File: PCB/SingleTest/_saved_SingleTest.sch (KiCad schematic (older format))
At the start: 5 parts

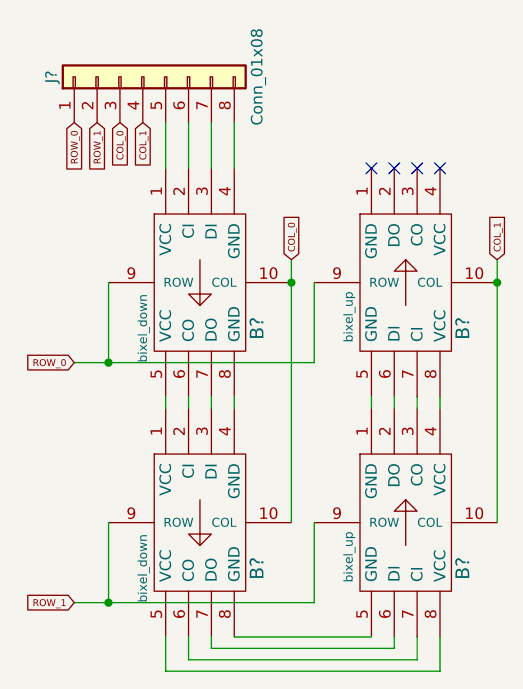
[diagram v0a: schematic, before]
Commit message: Adding single test
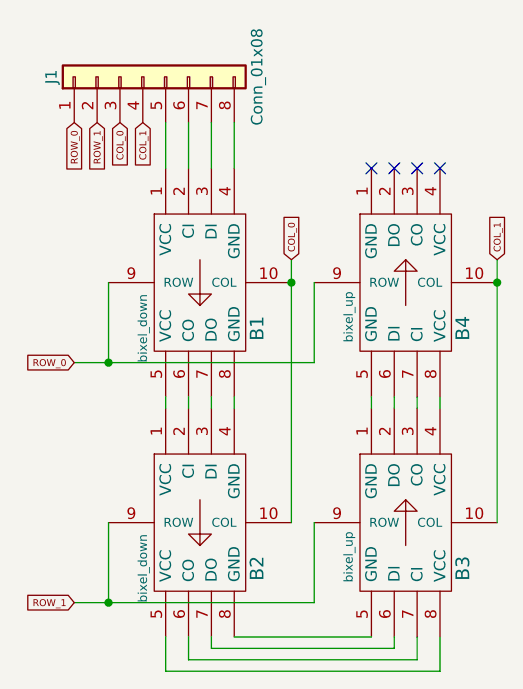
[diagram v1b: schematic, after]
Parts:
- B1, B2, B3, B4: renamed from B?; footprint (none) -> custom:bixel
- J1: renamed from J?; footprint (none) -> Socket_Strips:Socket_Strip_Straight_1x08_Pitch2.54mm
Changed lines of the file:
@@
 $EndDescr
 $Comp
-L bixel_down B?
+L bixel_down B1
 U 1 1 5B36BF26
 P 2600 3400
-F 0 "B?" V 2850 3200 60  0000 C CNN
+F 0 "B1" V 2850 3200 60  0000 C CNN
 F 1 "bixel_down" V 2350 3200 39  0000 C CNN
-F 2 "" H 2600 3400 60  0001 C CNN
+F 2 "custom:bixel" H 2600 3400 60  0001 C CNN
 F 3 "" H 2600 3400 60  0001 C CNN
 	1    2600 3400
@@
 $EndComp
 $Comp
-L bixel_up B?
+L bixel_up B4
 U 1 1 5B36BF6D
 P 3500 3400
-F 0 "B?" V 3750 3200 60  0000 C CNN
+F 0 "B4" V 3750 3200 60  0000 C CNN
 F 1 "bixel_up" V 3250 3250 39  0000 C CNN
-F 2 "" H 3500 3400 60  0001 C CNN
+F 2 "custom:bixel" H 3500 3400 60  0001 C CNN
 F 3 "" H 3500 3400 60  0001 C CNN
 	1    3500 3400
@@
 $EndComp
 $Comp
-L bixel_down B?
+L bixel_down B2
 U 1 1 5B36BFAC
 P 2600 4450
-F 0 "B?" V 2850 4250 60  0000 C CNN
+F 0 "B2" V 2850 4250 60  0000 C CNN
 F 1 "bixel_down" V 2350 4250 39  0000 C CNN
-F 2 "" H 2600 4450 60  0001 C CNN
+F 2 "custom:bixel" H 2600 4450 60  0001 C CNN
 F 3 "" H 2600 4450 60  0001 C CNN
 	1    2600 4450
@@
 $EndComp
 $Comp
-L bixel_up B?
+L bixel_up B3
 U 1 1 5B36BFD9
 P 3500 4450
-F 0 "B?" V 3750 4250 60  0000 C CNN
+F 0 "B3" V 3750 4250 60  0000 C CNN
 F 1 "bixel_up" V 3250 4300 39  0000 C CNN
-F 2 "" H 3500 4450 60  0001 C CNN
+F 2 "custom:bixel" H 3500 4450 60  0001 C CNN
 F 3 "" H 3500 4450 60  0001 C CNN
 	1    3500 4450
@@
 NoConn ~ 3650 2900
 $Comp
-L Conn_01x08 J?
+L Conn_01x08 J1
 U 1 1 5B36C3AB
 P 2350 2500
-F 0 "J?" H 2350 2900 50  0000 C CNN
+F 0 "J1" H 2350 2900 50  0000 C CNN
 F 1 "Conn_01x08" H 2350 2000 50  0000 C CNN
-F 2 "" H 2350 2500 50  0001 C CNN
+F 2 "Socket_Strips:Socket_Strip_Straight_1x08_Pitch2.54mm" H 2350 2500 50  0001 C CNN
 F 3 "" H 2350 2500 50  0001 C CNN
 	1    2350 2500
